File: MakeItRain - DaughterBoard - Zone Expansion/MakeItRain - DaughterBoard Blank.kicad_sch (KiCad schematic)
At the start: 1 part, among them J1 Conn_02x15_Odd_Even

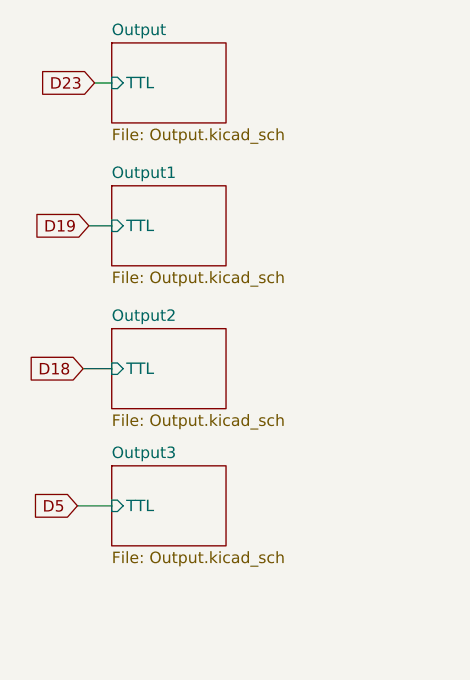
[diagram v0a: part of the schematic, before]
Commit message: adding support for Zone Expansion daughter board to FW finished daughter board design and pcb layout added fab files for zone expansion daughter board
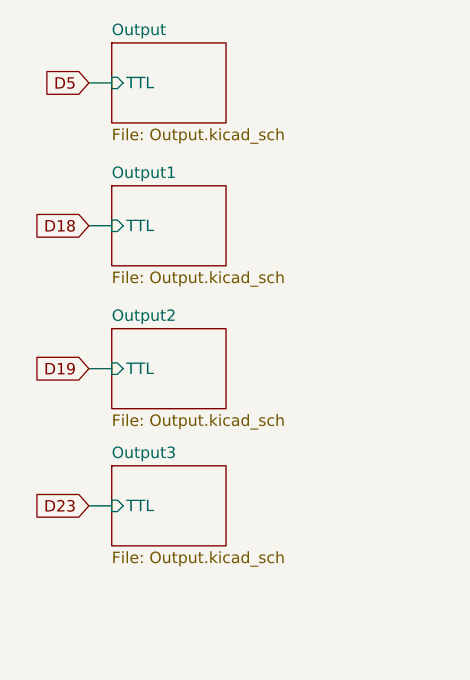
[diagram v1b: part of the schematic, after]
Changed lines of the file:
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@@
-    (stroke (width 0) (type default) (color 0 0 0 0))
-  )
-  (wire (pts (xy 137.16 111.125) (xy 140.97 111.125))
     (stroke (width 0) (type default) (color 0 0 0 0))
   )
@@
     (stroke (width 0) (type default) (color 0 0 0 0))
   )
-  (wire (pts (xy 139.065 64.135) (xy 140.97 64.135))
+  (wire (pts (xy 138.43 111.125) (xy 140.97 111.125))
     (stroke (width 0) (type default) (color 0 0 0 0))
   )
@@
     (stroke (width 0) (type default) (color 0 0 0 0))
   )
+  (wire (pts (xy 138.43 64.135) (xy 140.97 64.135))
+    (stroke (width 0) (type default) (color 0 0 0 0))
+  )
+  (wire (pts (xy 138.43 80.01) (xy 140.97 80.01))
+    (stroke (width 0) (type default) (color 0 0 0 0))
+  )
   (wire (pts (xy 237.49 156.845) (xy 237.49 159.385))
     (stroke (width 0) (type default) (color 0 0 0 0))
   )
-  (wire (pts (xy 233.68 136.525) (xy 237.49 136.525))
+  (wire (pts (xy 138.43 95.885) (xy 140.97 95.885))
     (stroke (width 0) (type default) (color 0 0 0 0))
   )
-  (wire (pts (xy 138.43 80.01) (xy 140.97 80.01))
+  (wire (pts (xy 233.68 136.525) (xy 237.49 136.525))
     (stroke (width 0) (type default) (color 0 0 0 0))
   )
@@
   )
   (wire (pts (xy 237.49 114.935) (xy 237.49 121.285))
-    (stroke (width 0) (type default) (color 0 0 0 0))
-  )
-  (wire (pts (xy 137.795 95.885) (xy 140.97 95.885))
     (stroke (width 0) (type default) (color 0 0 0 0))
   )
@@
     )
   )
-  (global_label "D18" (shape input) (at 137.795 95.885 180) (fields_autoplaced)
+  (global_label "D18" (shape input) (at 138.43 80.01 180) (fields_autoplaced)
     (effects (font (size 1.27 1.27)) (justify right))
-    (property "Intersheet References" "${INTERSHEET_REFS}" (id 0) (at 131.7818 95.8056 0)
+    (property "Intersheet References" "${INTERSHEET_REFS}" (id 0) (at 132.4168 79.9306 0)
       (effects (font (size 1.27 1.27)) (justify right) hide)
     )
@@
     )
   )
-  (global_label "D19" (shape input) (at 138.43 80.01 180) (fields_autoplaced)
+  (global_label "D19" (shape input) (at 138.43 95.885 180) (fields_autoplaced)
     (effects (font (size 1.27 1.27)) (justify right))
-    (property "Intersheet References" "${INTERSHEET_REFS}" (id 0) (at 132.4168 79.9306 0)
+    (property "Intersheet References" "${INTERSHEET_REFS}" (id 0) (at 132.4168 95.8056 0)
       (effects (font (size 1.27 1.27)) (justify right) hide)
     )
@@
     )
   )
-  (global_label "D5" (shape input) (at 137.16 111.125 180) (fields_autoplaced)
+  (global_label "D5" (shape input) (at 138.43 64.135 180) (fields_autoplaced)
     (effects (font (size 1.27 1.27)) (justify right))
-    (property "Intersheet References" "${INTERSHEET_REFS}" (id 0) (at 132.3563 111.0456 0)
+    (property "Intersheet References" "${INTERSHEET_REFS}" (id 0) (at 133.6263 64.0556 0)
       (effects (font (size 1.27 1.27)) (justify right) hide)
     )
@@
     )
   )
-  (global_label "D23" (shape input) (at 139.065 64.135 180) (fields_autoplaced)
+  (global_label "D23" (shape input) (at 138.43 111.125 180) (fields_autoplaced)
     (effects (font (size 1.27 1.27)) (justify right))
-    (property "Intersheet References" "${INTERSHEET_REFS}" (id 0) (at 133.0518 64.0556 0)
+    (property "Intersheet References" "${INTERSHEET_REFS}" (id 0) (at 132.4168 111.0456 0)
       (effects (font (size 1.27 1.27)) (justify right) hide)
     )

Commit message: updating some routes, updating the already done daughterboard and updating the blank layout for both.
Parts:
- removed J1: Conn_02x15_Odd_Even, Connector_PinHeader_2.54mm:PinHeader_2x15_P2.54mm_Vertical, symbol Connector_Generic:Conn_02x15_Odd_Even
- added J1: Conn_02x14_Odd_Even, Connector_PinHeader_2.54mm:PinHeader_2x14_P2.54mm_Vertical, symbol Connector_Generic:Conn_02x14_Odd_Even
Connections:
- net +3V3: now also J1.11 (Pin_11), J1.13 (Pin_13), J1.15 (Pin_15), J1.17 (Pin_17)
- net +VDC: now also J1.1 (Pin_1), J1.3 (Pin_3), J1.5 (Pin_5), J1.7 (Pin_7), J1.9 (Pin_9)
- net D18: now also J1.20 (Pin_20)
- net D19: now also J1.18 (Pin_18)
- net D23: now also J1.16 (Pin_16)
- net GND: now also J1.19 (Pin_19), J1.21 (Pin_21), J1.23 (Pin_23), J1.25 (Pin_25), J1.27 (Pin_27)
- net RX: now also J1.28 (Pin_28)
- net TX: now also J1.26 (Pin_26)
- new net D16: J1.24 (Pin_24)
- new net D17: J1.22 (Pin_22)
- new net D26: J1.14 (Pin_14)
- new net SCL: J1.2 (Pin_2)
- new net SDA: J1.4 (Pin_4)
- new net Z5: J1.12 (Pin_12)
- new net Z6: J1.10 (Pin_10)
- new net Z7: J1.8 (Pin_8)
- new net Z8: J1.6 (Pin_6)

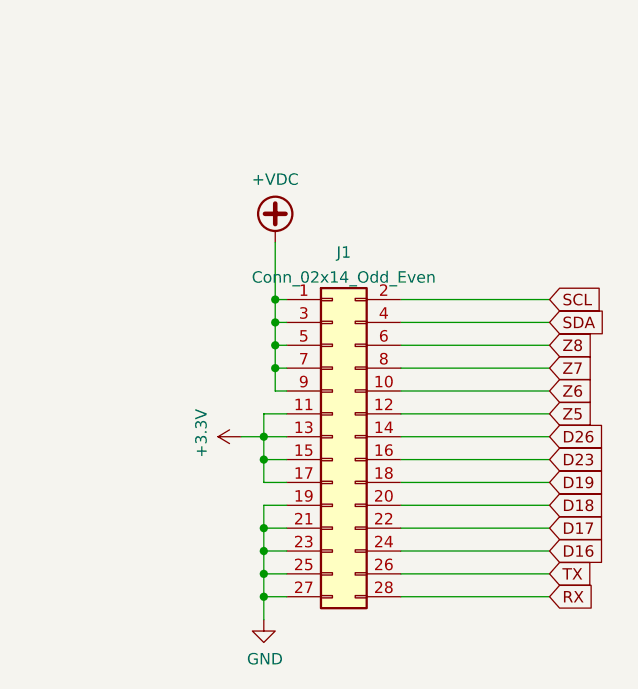
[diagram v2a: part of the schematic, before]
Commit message: MakeItRain * Main Board Fixed Routing. * replaced Opamp with the part that i can get as the old one is EOL * generated all the fab files i need. * updated the daughter plug witht eh i2c ttl flip * fixed I2C issues * DRC'ed the board
MakeItRain - DaughterBoard - Zone Expansion
* updated the daughter plug witht eh i2c ttl flip
* fixed some of the routings
* generated new fab files
* DRC'ed the board
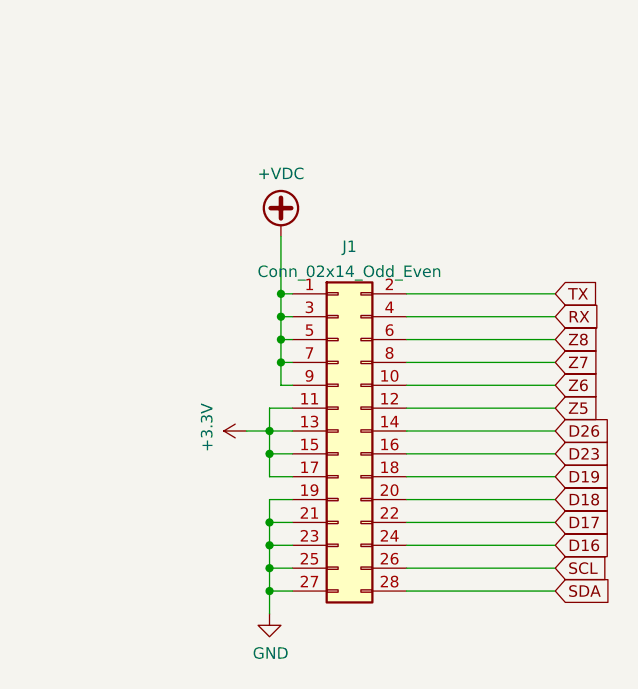
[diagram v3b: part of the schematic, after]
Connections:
- net RX: now also J1.4 (Pin_4); no longer J1.28 (Pin_28)
- net SCL: now also J1.26 (Pin_26); no longer J1.2 (Pin_2)
- net SDA: now also J1.28 (Pin_28); no longer J1.4 (Pin_4)
- net TX: now also J1.2 (Pin_2); no longer J1.26 (Pin_26)
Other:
- moved on the sheet: J1
